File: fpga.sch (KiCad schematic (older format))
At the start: 36 parts, among them IC1 EP4CE10F17, J1 Pinheader_2x5_TH_WALL, U21 EPCS4, Y3 Crystal_GND24

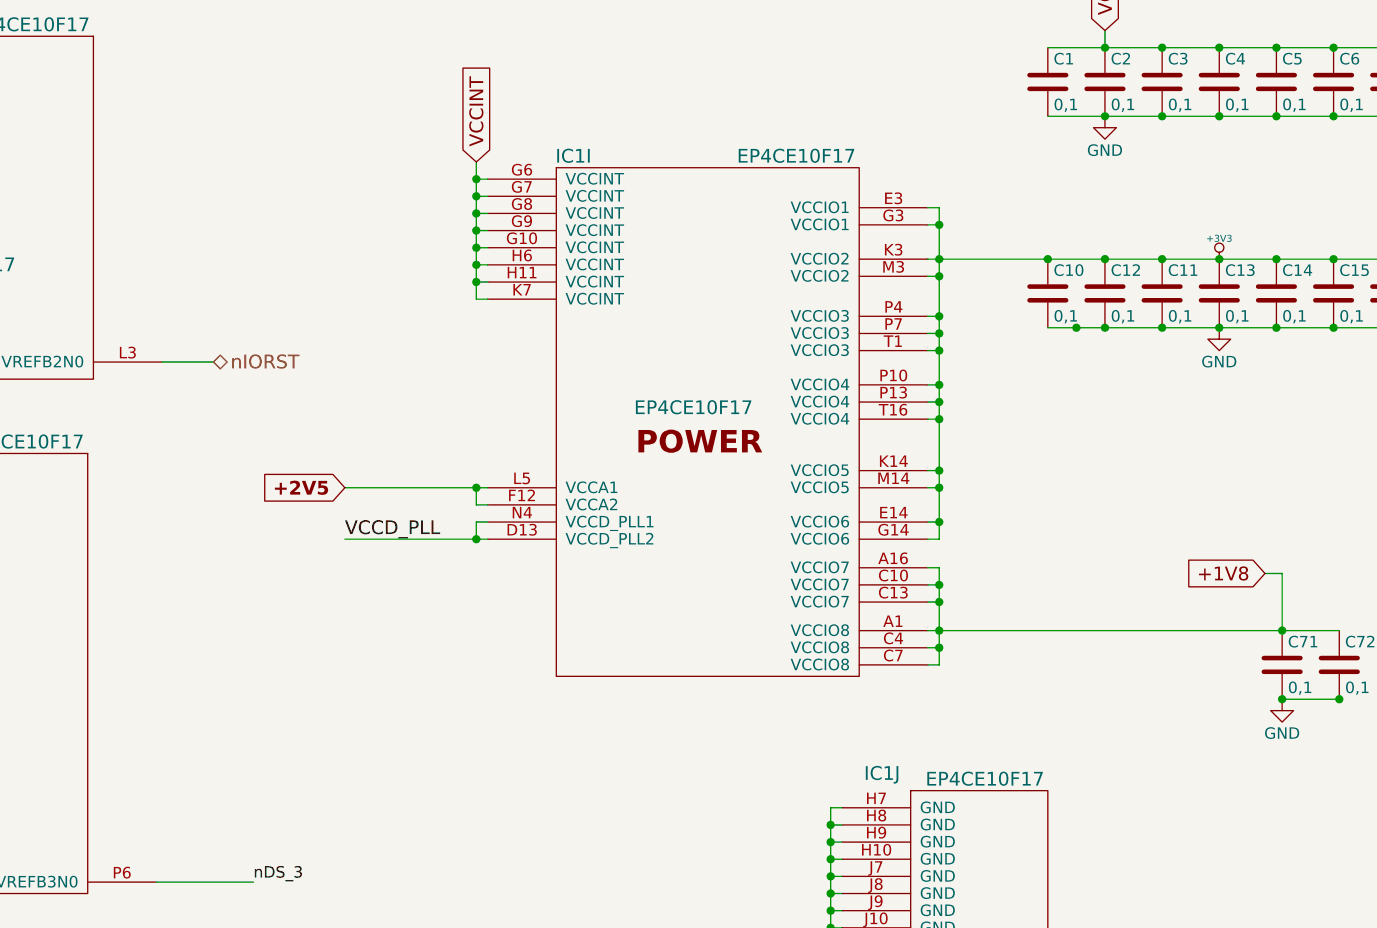
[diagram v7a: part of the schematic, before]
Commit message: VCCD_PLL routed
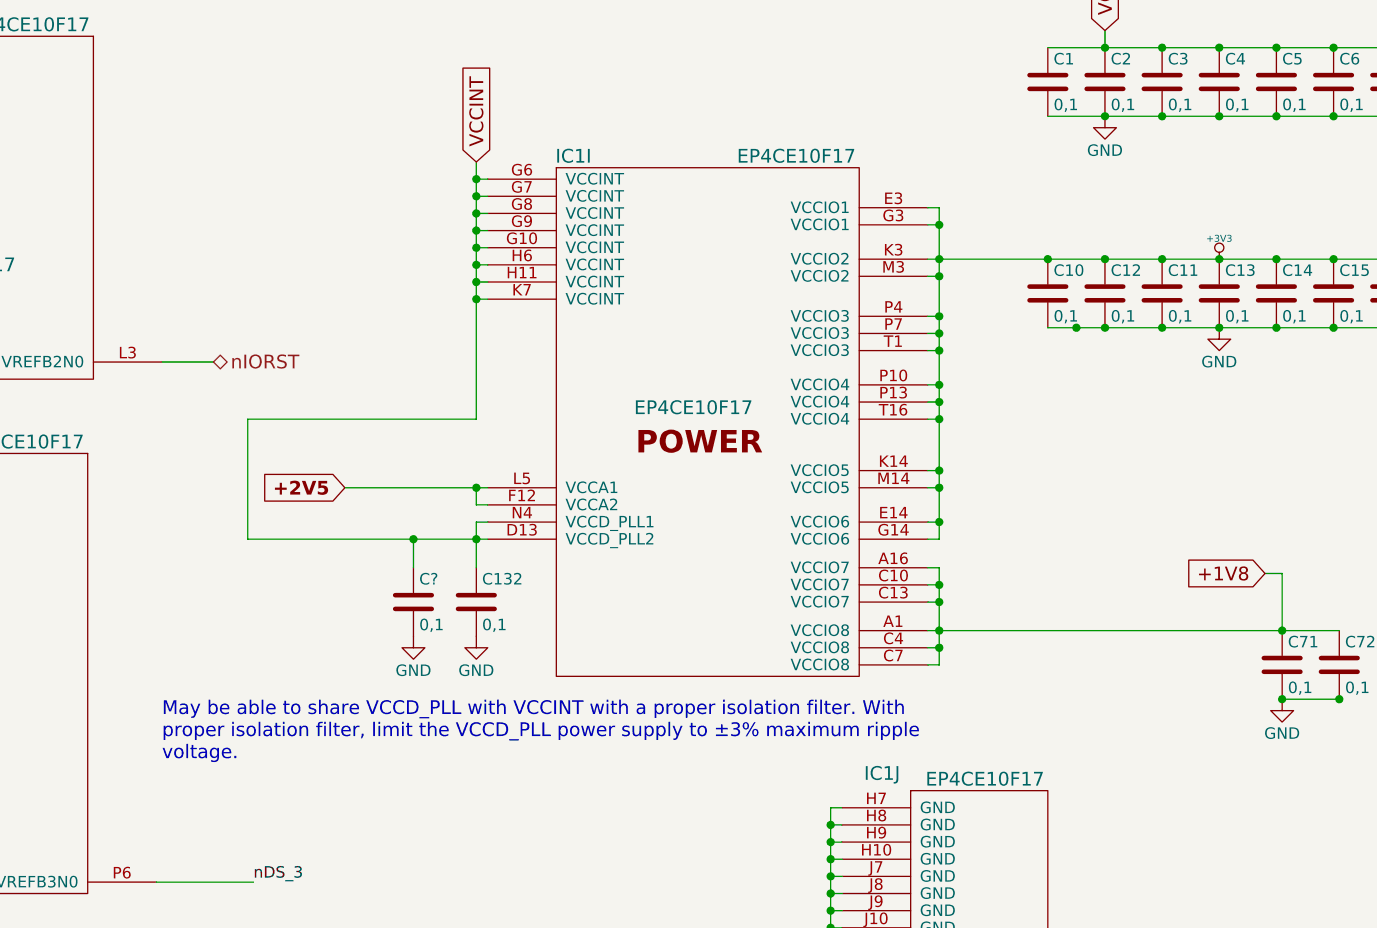
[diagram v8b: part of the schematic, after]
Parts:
- added C132, C?: 0,1, Capacitors_SMD:C_0402, symbol C
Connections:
- net labels removed: VCCD_PLL
- wire segments 139 -> 142
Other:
- note added: "May be able to share VCCD_PLL with VCCINT with a proper isolation filter. With\nproper isolation filter, limit the VCCD_PLL power supply to ±3% maximum ripple\nvoltage."
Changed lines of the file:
@@
 $EndComp
 $Comp
-L GND #PWR01
+L GND #PWR13
 U 1 1 5807C448
 P 12075 6725
-F 0 "#PWR01" H 12075 6475 50  0001 C CNN
+F 0 "#PWR13" H 12075 6475 50  0001 C CNN
 F 1 "GND" H 12075 6575 50  0000 C CNN
 F 2 "" H 12075 6725 50  0000 C CNN
@@
 Text GLabel 10525 1600 1    60   Input ~ 0
 VCCINT
-Text Label 9950 3250 0    60   ~ 0
-VCCD_PLL
 Text Label 3650 1875 0    60   ~ 0
 VREFB1N0
@@
 $EndComp
 $Comp
-L GND #PWR02
+L GND #PWR5
 U 1 1 57F7A288
 P 2675 3000
-F 0 "#PWR02" H 2675 2750 50  0001 C CNN
+F 0 "#PWR5" H 2675 2750 50  0001 C CNN
 F 1 "GND" H 2675 2850 50  0000 C CNN
 F 2 "" H 2675 3000 50  0000 C CNN
@@
 NoConn ~ 2600 2775
 $Comp
-L +3V3 #PWR03
+L +3V3 #PWR15
 U 1 1 57F8D5C6
 P 13775 2025
-F 0 "#PWR03" H 13875 2075 20  0001 C CNN
+F 0 "#PWR15" H 13875 2075 20  0001 C CNN
 F 1 "+3V3" H 13775 2115 30  0000 C CNN
 F 2 "" H 13775 2025 60  0000 C CNN
@@
 $EndComp
 $Comp
-L GND #PWR04
+L GND #PWR16
 U 1 1 57F8FD8F
 P 13775 2325
-F 0 "#PWR04" H 13775 2075 50  0001 C CNN
+F 0 "#PWR16" H 13775 2075 50  0001 C CNN
 F 1 "GND" H 13775 2175 50  0000 C CNN
 F 2 "" H 13775 2325 50  0000 C CNN
@@
 $EndComp
 $Comp
-L GND #PWR05
+L GND #PWR14
 U 1 1 57F90743
 P 13275 1400
-F 0 "#PWR05" H 13275 1150 50  0001 C CNN
+F 0 "#PWR14" H 13275 1150 50  0001 C CNN
 F 1 "GND" H 13275 1250 50  0000 C CNN
 F 2 "" H 13275 1400 50  0000 C CNN
@@
 Wire Wire Line
 	10525 2200 10575 2200
-Wire Wire Line
-	10525 1600 10525 2200
 Connection ~ 10525 1675
 Wire Wire Line
@@
 	10575 3175 10525 3175
 Wire Wire Line
-	9950 3250 10575 3250
+	9525 3250 10575 3250
 Wire Wire Line
 	3625 1125 4125 1125
@@
 $EndComp
 $Comp
-L GND #PWR06
+L GND #PWR2
 U 1 1 58612A86
 P 1700 4125
-F 0 "#PWR06" H 1700 3875 50  0001 C CNN
+F 0 "#PWR2" H 1700 3875 50  0001 C CNN
 F 1 "GND" H 1700 3975 50  0000 C CNN
 F 2 "" H 1700 4125 50  0000 C CNN
@@
 $EndComp
 $Comp
-L +3V3 #PWR07
+L +3V3 #PWR3
 U 1 1 586140D5
 P 2650 3775
-F 0 "#PWR07" H 2750 3825 20  0001 C CNN
+F 0 "#PWR3" H 2750 3825 20  0001 C CNN
 F 1 "+3V3" H 2650 3865 30  0000 C CNN
 F 2 "" H 2650 3775 60  0000 C CNN
@@
 Connection ~ 2650 3825
 $Comp
-L +3V3 #PWR08
+L +3V3 #PWR1
 U 1 1 58614C3F
 P 1575 4025
-F 0 "#PWR08" H 1675 4075 20  0001 C CNN
+F 0 "#PWR1" H 1675 4075 20  0001 C CNN
 F 1 "+3V3" V 1625 4075 30  0000 C CNN
 F 2 "" H 1575 4025 60  0000 C CNN
@@
 $EndComp
 $Comp
-L GND #PWR09
+L GND #PWR4
 U 1 1 586161B6
 P 2650 4500
-F 0 "#PWR09" H 2650 4250 50  0001 C CNN
+F 0 "#PWR4" H 2650 4250 50  0001 C CNN
 F 1 "GND" H 2650 4350 50  0000 C CNN
 F 2 "" H 2650 4500 50  0000 C CNN
@@
 $EndComp
 $Comp
-L GND #PWR010
+L GND #PWR17
 U 1 1 5883481A
 P 14050 3950
-F 0 "#PWR010" H 14050 3700 50  0001 C CNN
+F 0 "#PWR17" H 14050 3700 50  0001 C CNN
 F 1 "GND" H 14050 3800 50  0000 C CNN
 F 2 "" H 14050 3950 50  0000 C CNN
@@
 $EndComp
 $Comp
-L GND #PWR011
+L GND #PWR8
 U 1 1 58A8994C
 P 4050 4225
-F 0 "#PWR011" H 4050 3975 50  0001 C CNN
+F 0 "#PWR8" H 4050 3975 50  0001 C CNN
 F 1 "GND" H 4050 4075 50  0000 C CNN
 F 2 "" H 4050 4225 50  0000 C CNN
@@
 $EndComp
 $Comp
-L GND #PWR012
+L GND #PWR6
 U 1 1 58A8A622
 P 3425 4200
-F 0 "#PWR012" H 3425 3950 50  0001 C CNN
+F 0 "#PWR6" H 3425 3950 50  0001 C CNN
 F 1 "GND" H 3425 4050 50  0000 C CNN
 F 2 "" H 3425 4200 50  0000 C CNN
@@
 Connection ~ 4050 3725
 $Comp
-L GND #PWR013
+L GND #PWR9
 U 1 1 58A8A9F2
 P 4700 4500
-F 0 "#PWR013" H 4700 4250 50  0001 C CNN
+F 0 "#PWR9" H 4700 4250 50  0001 C CNN
 F 1 "GND" H 4700 4350 50  0000 C CNN
 F 2 "" H 4700 4500 50  0000 C CNN
@@
 nSTATUS
 $Comp
-L GND #PWR014
+L GND #PWR11
 U 1 1 58ACB779
 P 4975 1825
-F 0 "#PWR014" H 4975 1575 50  0001 C CNN
+F 0 "#PWR11" H 4975 1575 50  0001 C CNN
 F 1 "GND" H 4975 1675 50  0000 C CNN
 F 2 "" H 4975 1825 50  0000 C CNN
@@
 Connection ~ 12550 1875
 $Comp
-L +3V3 #PWR015
+L +3V3 #PWR10
 U 1 1 58AD9DC7
 P 4725 750
-F 0 "#PWR015" H 4825 800 20  0001 C CNN
+F 0 "#PWR10" H 4825 800 20  0001 C CNN
 F 1 "+3V3" H 4725 840 30  0000 C CNN
 F 2 "" H 4725 750 60  0000 C CNN
@@
 Connection ~ 4725 800
 Wire Wire Line
-	10525 3175 10525 3250
+	10525 3175 10525 3375
 Connection ~ 10525 3250
 $Comp
-L +3V3 #PWR016
+L +3V3 #PWR7
 U 1 1 58B48267
 P 3850 3575
-F 0 "#PWR016" H 3950 3625 20  0001 C CNN
+F 0 "#PWR7" H 3950 3625 20  0001 C CNN
 F 1 "+3V3" H 3850 3665 30  0000 C CNN
 F 2 "" H 3850 3575 60  0000 C CNN
@@
 Text GLabel 9950 3025 0    60   Input ~ 12
 +2V5
+Text Notes 9150 4225 0    60   ~ 0
+May be able to share VCCD_PLL with VCCINT with a proper isolation filter. With\nproper isolation filter, limit the VCCD_PLL power supply to ±3% maximum ripple\nvoltage.
+Connection ~ 10525 2200
+$Comp
+L C C132
+U 1 1 58B4A4B4
+P 10525 3525
+F 0 "C132" H 10550 3625 50  0000 L CNN
+F 1 "0,1" H 10550 3425 50  0000 L CNN
+F 2 "Capacitors_SMD:C_0402" H 10563 3375 50  0001 C CNN
+F 3 "" H 10525 3525 50  0000 C CNN
+	1    10525 3525
+	1    0    0    -1
+$EndComp
+$Comp
+L GND #PWR12
+U 1 1 58B4A83F
+P 10525 3675
+F 0 "#PWR12" H 10525 3425 50  0001 C CNN
+F 1 "GND" H 10525 3525 50  0000 C CNN
+F 2 "" H 10525 3675 50  0000 C CNN
+F 3 "" H 10525 3675 50  0000 C CNN
+	1    10525 3675
+	1    0    0    -1
+$EndComp
+Wire Wire Line
+	10525 1600 10525 2725
+Wire Wire Line
+	9525 3250 9525 2725
+Wire Wire Line
+	9525 2725 10525 2725
+$Comp
+L C C?
+U 1 1 58B4B61E
+P 10250 3525
+F 0 "C?" H 10275 3625 50  0000 L CNN
+F 1 "0,1" H 10275 3425 50  0000 L CNN
+F 2 "Capacitors_SMD:C_0402" H 10288 3375 50  0001 C CNN
+F 3 "" H 10250 3525 50  0000 C CNN
+	1    10250 3525
+	1    0    0    -1
+$EndComp
+Wire Wire Line
+	10250 3375 10250 3250
+Connection ~ 10250 3250
+$Comp
+L GND #PWR?
+U 1 1 58B4B860
+P 10250 3675
+F 0 "#PWR?" H 10250 3425 50  0001 C CNN
+F 1 "GND" H 10250 3525 50  0000 C CNN
+F 2 "" H 10250 3675 50  0000 C CNN
+F 3 "" H 10250 3675 50  0000 C CNN
+	1    10250 3675
+	1    0    0    -1
+$EndComp
 $EndSCHEMATC
